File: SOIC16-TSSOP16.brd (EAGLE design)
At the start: 20 x 22.9 mm, 7 parts

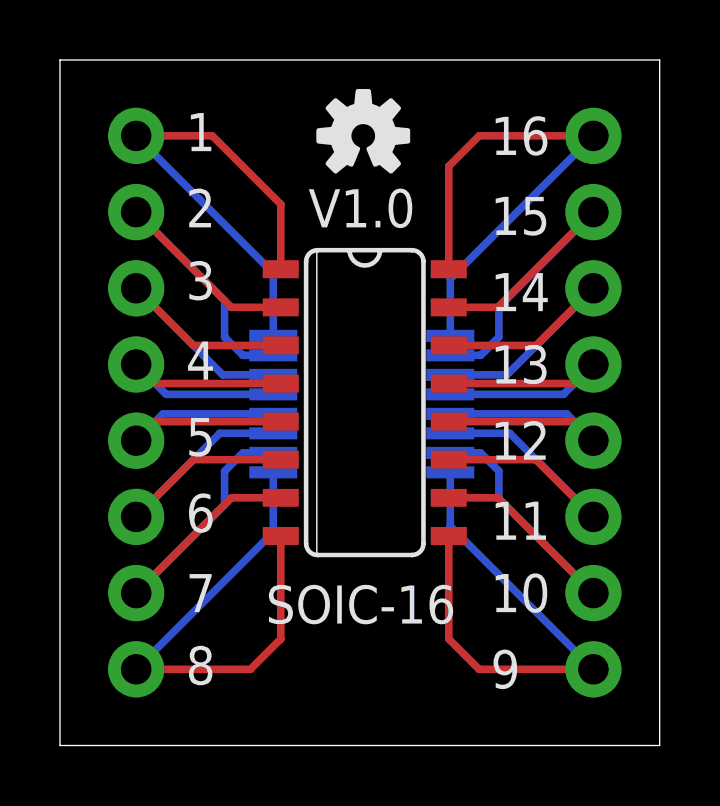
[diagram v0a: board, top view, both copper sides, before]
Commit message: Silk and board revision
Worked several silk screen issues and narrowed some boards.
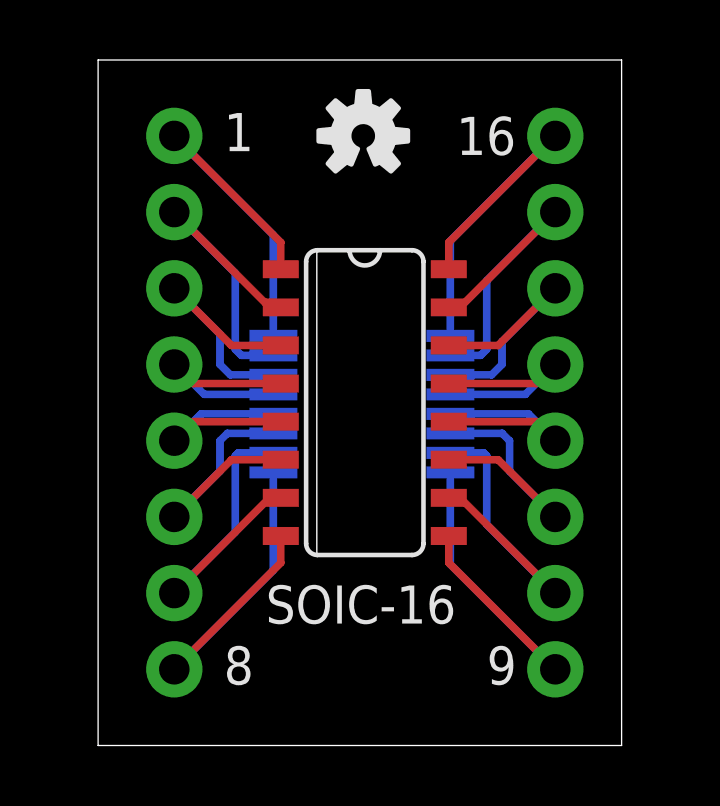
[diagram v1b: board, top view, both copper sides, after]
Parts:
- moved JP1 1.27 mm to (3.81, 7.62)
- moved JP2 1.27 mm to (16.5, 7.62)
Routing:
- net N$11: track 17.3 -> 14.0 mm
- net N$8: track 17.1 -> 13.8 mm
- net N$18: track 17.2 -> 13.9 mm
- net N$4: track 10.1 -> 7.53 mm
- net N$14: track 10.3 -> 7.73 mm
- net N$5: track 10.0 -> 7.48 mm
- net N$15: track 10.2 -> 7.68 mm
- net N$1: track 16.5 -> 13.9 mm
- net N$13: track 11.6 -> 9.48 mm
- net N$6: track 11.3 -> 9.39 mm
- net N$3: track 11.4 -> 9.43 mm
- net N$16: track 11.5 -> 9.59 mm
- net N$12: track 13.5 -> 11.7 mm
- net N$2: track 13.4 -> 11.6 mm
- net N$17: track 13.4 -> 11.6 mm
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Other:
- board size 20 x 22.9 mm -> 17.4 x 22.9 mm
- board text removed: "10"
- board text removed: "11"
- board text removed: "12"
- board text removed: "13"
- board text removed: "14"
- board text removed: "15"
- board text removed: "2"
- board text removed: "3"
- board text removed: "4"
- board text removed: "5"
- board text removed: "6"
- board text removed: "7"
- board text removed: "V1.0"
